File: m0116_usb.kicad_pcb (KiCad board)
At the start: 2 copper layers, 372.1 x 113.8 mm, 186 parts, among them J1 AVR-ISP-6, J2 Conn_01x04, J3 Conn_01x04, U1 ATmega32A-PU

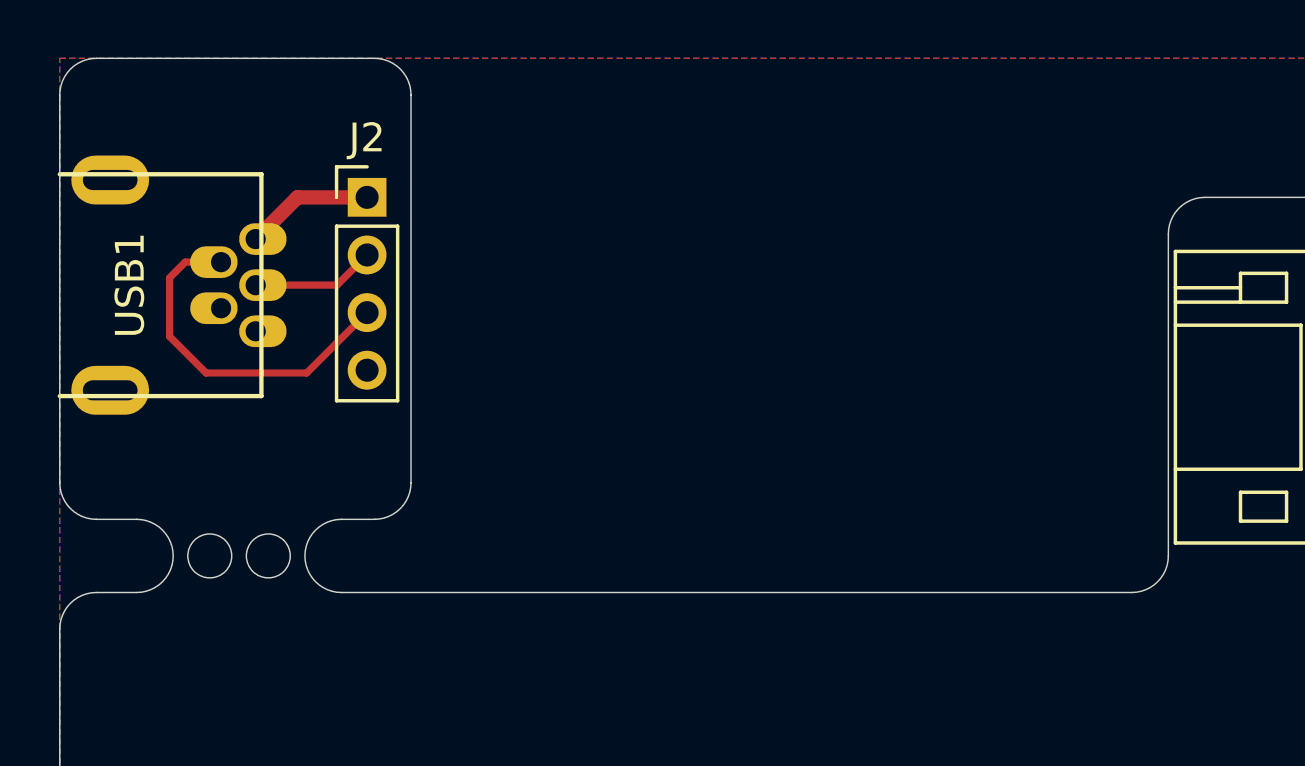
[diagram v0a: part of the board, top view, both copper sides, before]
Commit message: move the breakout pad to make JLC happy
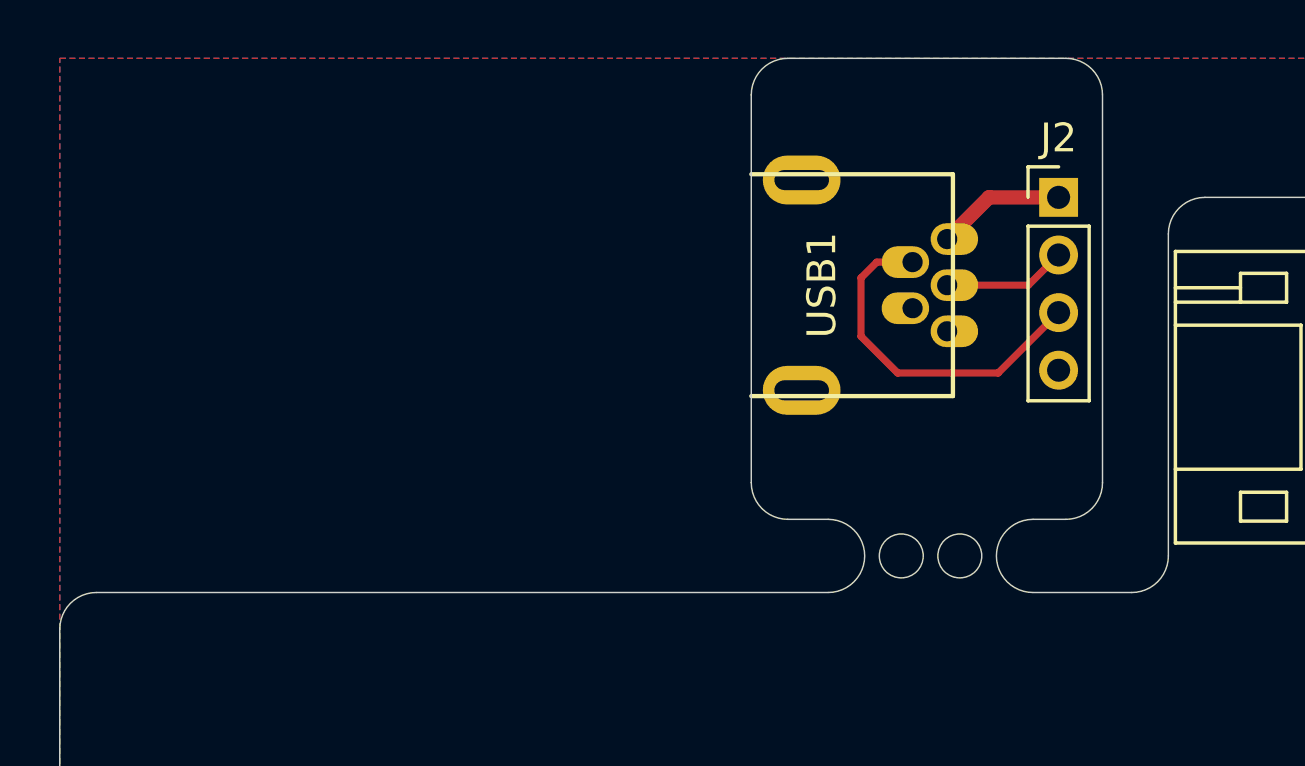
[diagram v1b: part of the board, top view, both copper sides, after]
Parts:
- moved J2 24.0 mm to (59.3, 77.2)
- moved USB1 24.0 mm to (48.6, 80.3)
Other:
- outline, holes or cut-outs redrawn

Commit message: fixed clearance issues with buttons
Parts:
- moved Reset 67.3 mm to (235.6, 85.3)
- moved Boot 66.9 mm to (235.6, 77.2)
- moved R1 66.6 mm to (229.9, 88.9)
- moved C4 9.66 mm to (250.7, 76.2)
- moved C5 9.66 mm to (250.7, 91.6)
- moved XTAL1 9.66 mm to (248.7, 81.4)
- moved C3 8.33 mm to (280.4, 73.8)
- moved U1 8.33 mm to (303.3, 76.5)
- moved C2 4.26 mm to (276.6, 94.2), turned to 270 degrees
- moved MX72 0.25 mm to (139.1, 79.5)
- renumbered Boot1 to Boot, Reset1 to Reset
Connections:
- U1 pad 3: row2 -> row1
- U1 pad 40: row1 -> row2
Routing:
- net boot: track 102.2 -> 27.5 mm
- net reset: track 220.1 -> 152.2 mm, vias 1 -> 0
- net +5V: track 389.1 -> 353.9 mm
- net row1: track 362.3 -> 386.5 mm
- net MOSI: track 91.1 -> 73.6 mm
- net row2: track 402.4 -> 386.8 mm
- net MISO: track 91.1 -> 76.2 mm
- net SCK: track 91.1 -> 78.9 mm
- net col3: track 283.3 -> 294.4 mm
- net col4: track 264.1 -> 275.2 mm
- net col15: track 136.9 -> 127.7 mm
- net col18: track 185.9 -> 176.8 mm
- net D-: track 74.1 -> 83.2 mm
- net col5: track 214.7 -> 206.2 mm
- net row3: track 392.3 -> 400.6 mm
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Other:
- board text added: "M0116 USB PCB rev2"
- board text removed: "M0116 USB PCB rev1"

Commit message: update
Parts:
- moved G*** 5.97 mm to (132.6, 170.8)
- moved G*** 5.97 mm to (155.6, 170.6)
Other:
- board text added: "github.com/kb-elmo/m0116_usb elmo.space"
